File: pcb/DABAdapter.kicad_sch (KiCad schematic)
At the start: 36 parts, among them J1 RFShield_OnePiece, J2 Ant, J3 Conn_01x06, J4 AudioJack3_Ground, J6 Conn_01x06, U1 SST25VF080B-50-4x-S2Ax, U3 abcdefg, U4 MIC5504-1.8YM5, Y1 19.2Mhz

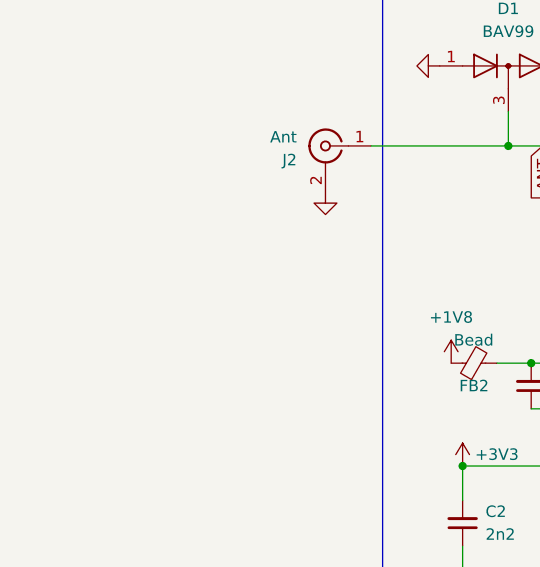
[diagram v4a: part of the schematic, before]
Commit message: Finishing touches
- Added image to readme
- Add Wuerth 3d model of the shield
- Add DAB logo to the pcb
- New board outline for the optional TRS antenna socket
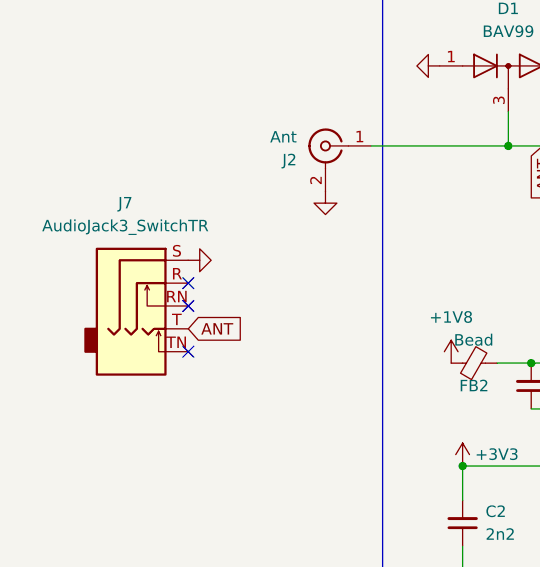
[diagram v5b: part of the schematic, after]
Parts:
- added J7: AudioJack3_SwitchTR, Connector_Audio:Jack_3.5mm_CUI_SJ2-3593D-SMT_Horizontal, symbol Connector_Audio:AudioJack3_SwitchTR
- J1, J3, J4, J6, U1: now left out of the parts list
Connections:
- net ANT: now also J7.T
- net GND: now also J7.S
- no-connect marks 0 -> 3
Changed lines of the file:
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@@
 		(color 0 0 0 0)
 	)
+	(no_connect
+		(at 39.37 76.2)
+	)
+	(no_connect
+		(at 39.37 81.28)
+	)
+	(no_connect
+		(at 39.37 73.66)
+	)
 	(wire
 		(pts
@@
 		)
 	)
+	(global_label "ANT"
+		(shape input)
+		(at 39.37 78.74 0)
+		(fields_autoplaced yes)
+		(effects
+			(font
+				(size 1.27 1.27)
+			)
+			(justify left)
+		)
+		(property "Intersheetrefs" "${INTERSHEET_REFS}"
+			(at 45.7419 78.74 0)
+			(effects
+				(font
+					(size 1.27 1.27)
+				)
+				(justify left)
+				(hide yes)
+			)
+		)
+	)
 	(global_label "NVSSB"
 		(shape input)
@@
 		(unit 1)
 		(exclude_from_sim no)
-		(in_bom yes)
+		(in_bom no)
 		(on_board yes)
 		(dnp yes)
@@
 			)
 		)
-		(property "Datasheet" " ~"
+		(property "Datasheet" "~"
 			(at 54.61 58.42 0)
 			(effects
@@
 		(unit 1)
 		(exclude_from_sim no)
-		(in_bom yes)
+		(in_bom no)
 		(on_board yes)
 		(dnp no)
@@
 		(unit 1)
 		(exclude_from_sim no)
-		(in_bom yes)
+		(in_bom no)
 		(on_board yes)
 		(dnp no)
@@
 		(unit 1)
 		(exclude_from_sim no)
-		(in_bom yes)
+		(in_bom no)
 		(on_board yes)
 		(dnp no)
@@
 	)
 	(symbol
+		(lib_id "Connector_Audio:AudioJack3_SwitchTR")
+		(at 34.29 73.66 0)
+		(unit 1)
+		(exclude_from_sim no)
+		(in_bom no)
+		(on_board yes)
+		(dnp no)
+		(fields_autoplaced yes)
+		(property "Reference" "J7"
+			(at 32.385 64.77 0)
+			(effects
+				(font
+					(size 1.27 1.27)
+				)
+			)
+		)
+		(property "Value" "AudioJack3_SwitchTR"
+			(at 32.385 67.31 0)
+			(effects
+				(font
+					(size 1.27 1.27)
+				)
+			)
+		)
+		(property "Footprint" "Connector_Audio:Jack_3.5mm_CUI_SJ2-3593D-SMT_Horizontal"
+			(at 34.29 73.66 0)
+			(effects
+				(font
+					(size 1.27 1.27)
+				)
+				(hide yes)
+			)
+		)
+		(property "Datasheet" "~"
+			(at 34.29 73.66 0)
+			(effects
+				(font
+					(size 1.27 1.27)
+				)
+				(hide yes)
+			)
+		)
+		(property "Description" "Audio Jack, 3 Poles (Stereo / TRS), Switched TR Poles (Normalling)"
+			(at 34.29 73.66 0)
+			(effects
+				(font
+					(size 1.27 1.27)
+				)
+				(hide yes)
+			)
+		)
+		(pin "S"
+		)
+		(pin "RN"
+		)
+		(pin "R"
+		)
+		(pin "TN"
+		)
+		(pin "T"
+		)
+		(instances
+			(project ""
+				(path "/60db4cc3-609c-4934-a7c7-72b268f417a1"
+					(reference "J7")
+					(unit 1)
+				)
+			)
+		)
+	)
+	(symbol
 		(lib_id "power:GND")
 		(at 171.45 55.88 0)
@@
 	)
 	(symbol
+		(lib_id "power:GND")
+		(at 39.37 71.12 90)
+		(unit 1)
+		(exclude_from_sim no)
+		(in_bom yes)
+		(on_board yes)
+		(dnp no)
+		(fields_autoplaced yes)
+		(property "Reference" "#PWR09"
+			(at 45.72 71.12 0)
+			(effects
+				(font
+					(size 1.27 1.27)
+				)
+				(hide yes)
+			)
+		)
+		(property "Value" "GND"
+			(at 45.72 71.12 0)
+			(effects
+				(font
+					(size 1.27 1.27)
+				)
+				(hide yes)
+			)
+		)
+		(property "Footprint" ""
+			(at 39.37 71.12 0)
+			(effects
+				(font
+					(size 1.27 1.27)
+				)
+				(hide yes)
+			)
+		)
+		(property "Datasheet" ""
+			(at 39.37 71.12 0)
+			(effects
+				(font
+					(size 1.27 1.27)
+				)
+				(hide yes)
+			)
+		)
+		(property "Description" ""
+			(at 39.37 71.12 0)
+			(effects
+				(font
+					(size 1.27 1.27)
+				)
+				(hide yes)
+			)
+		)
+		(pin "1"
+		)
+		(instances
+			(project "DABAdapter"
+				(path "/60db4cc3-609c-4934-a7c7-72b268f417a1"
+					(reference "#PWR09")
+					(unit 1)
+				)
+			)
+		)
+	)
+	(symbol
 		(lib_id "power:+1V8")
 		(at 97.79 104.14 0)
@@
 		(unit 1)
 		(exclude_from_sim no)
-		(in_bom yes)
+		(in_bom no)
 		(on_board yes)
 		(dnp no)
